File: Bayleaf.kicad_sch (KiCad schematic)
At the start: 68 parts, among them SW1 SW_SPDT, U1 Nice_Nano_V2

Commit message: v1 power management
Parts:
- added J1: Conn_01x02_Socket, Connector_PinHeader_2.54mm:PinHeader_1x02_P2.54mm_Vertical, symbol Connector:Conn_01x02_Socket
- added J2: Conn_01x02_Socket, Connector_JST:JST_SH_SM02B-SRSS-TB_1x02-1MP_P1.00mm_Horizontal, symbol Connector:Conn_01x02_Socket
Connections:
- net GND: now reaches U1.23 (GND)
- net GND: now also U1.3 (GND), U1.4 (GND), J1.1 (Pin_1), J2.2 (Pin_2)
- net +BATT: now reaches U1.24 (B+)
- net +BATT: now also SW1.2 (B)
- net at SW1.3 (C): now also J1.2 (Pin_2), J2.1 (Pin_1)
- no-connect marks 0 -> 1
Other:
- moved on the sheet: H1, H2, H3, H4, H5, H6

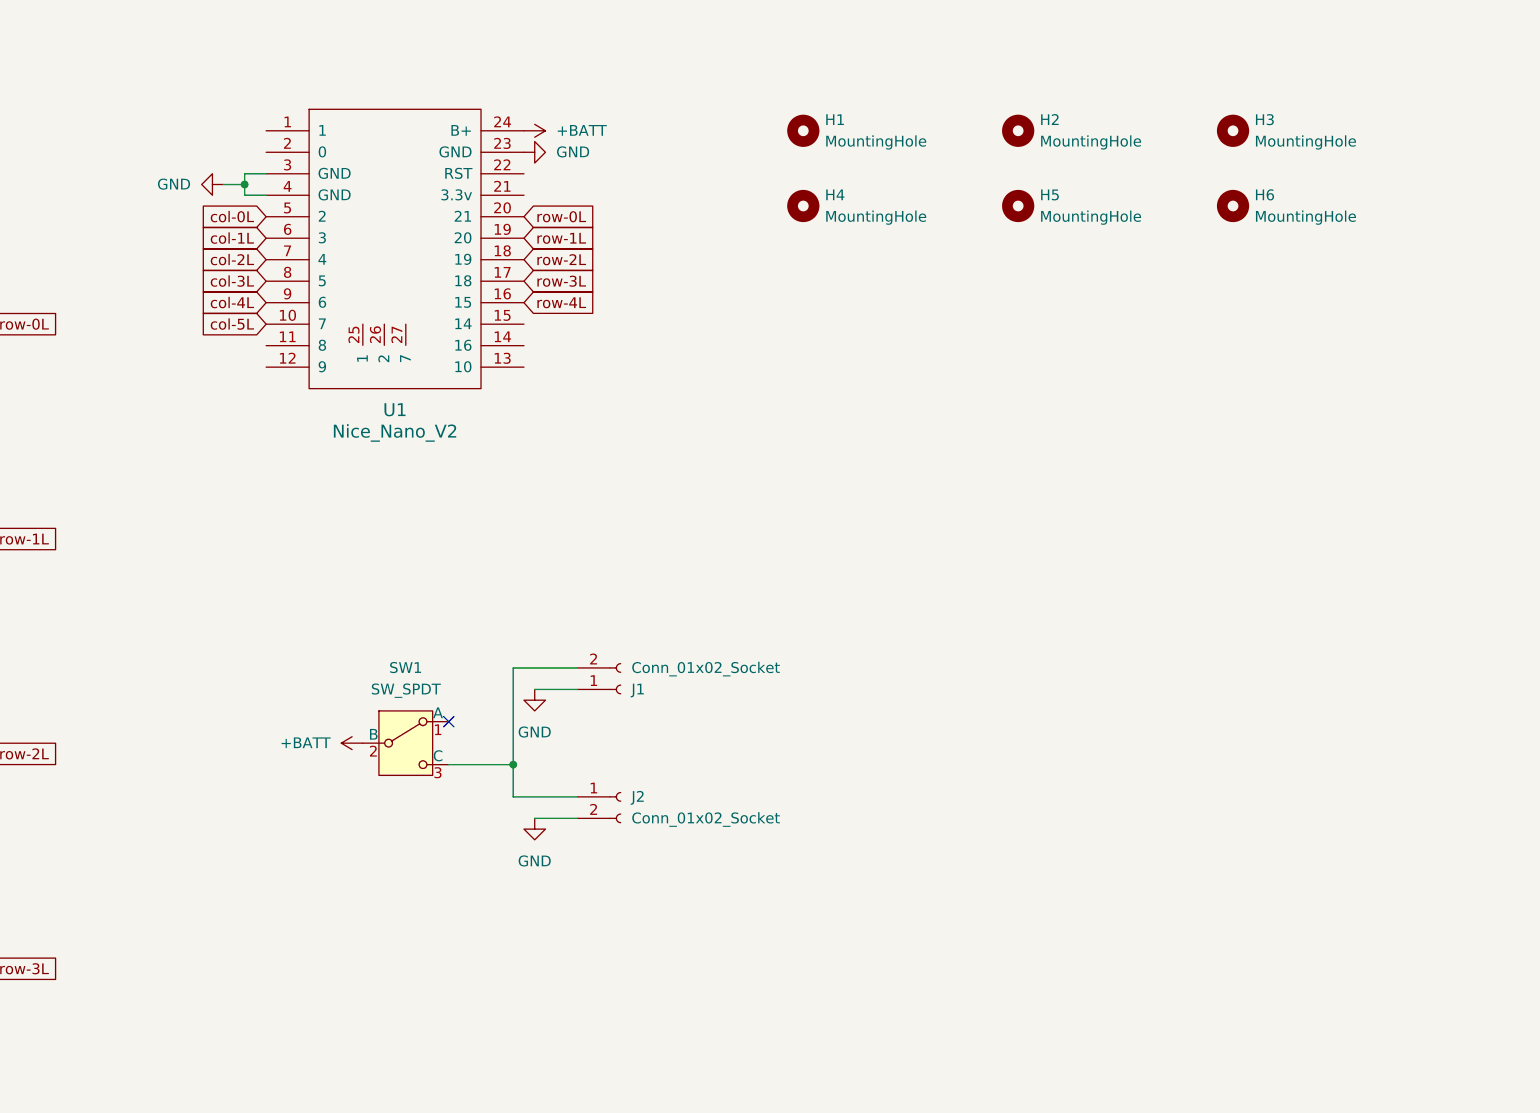
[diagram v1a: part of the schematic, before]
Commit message: Add rst, flags, logo, mounting hole
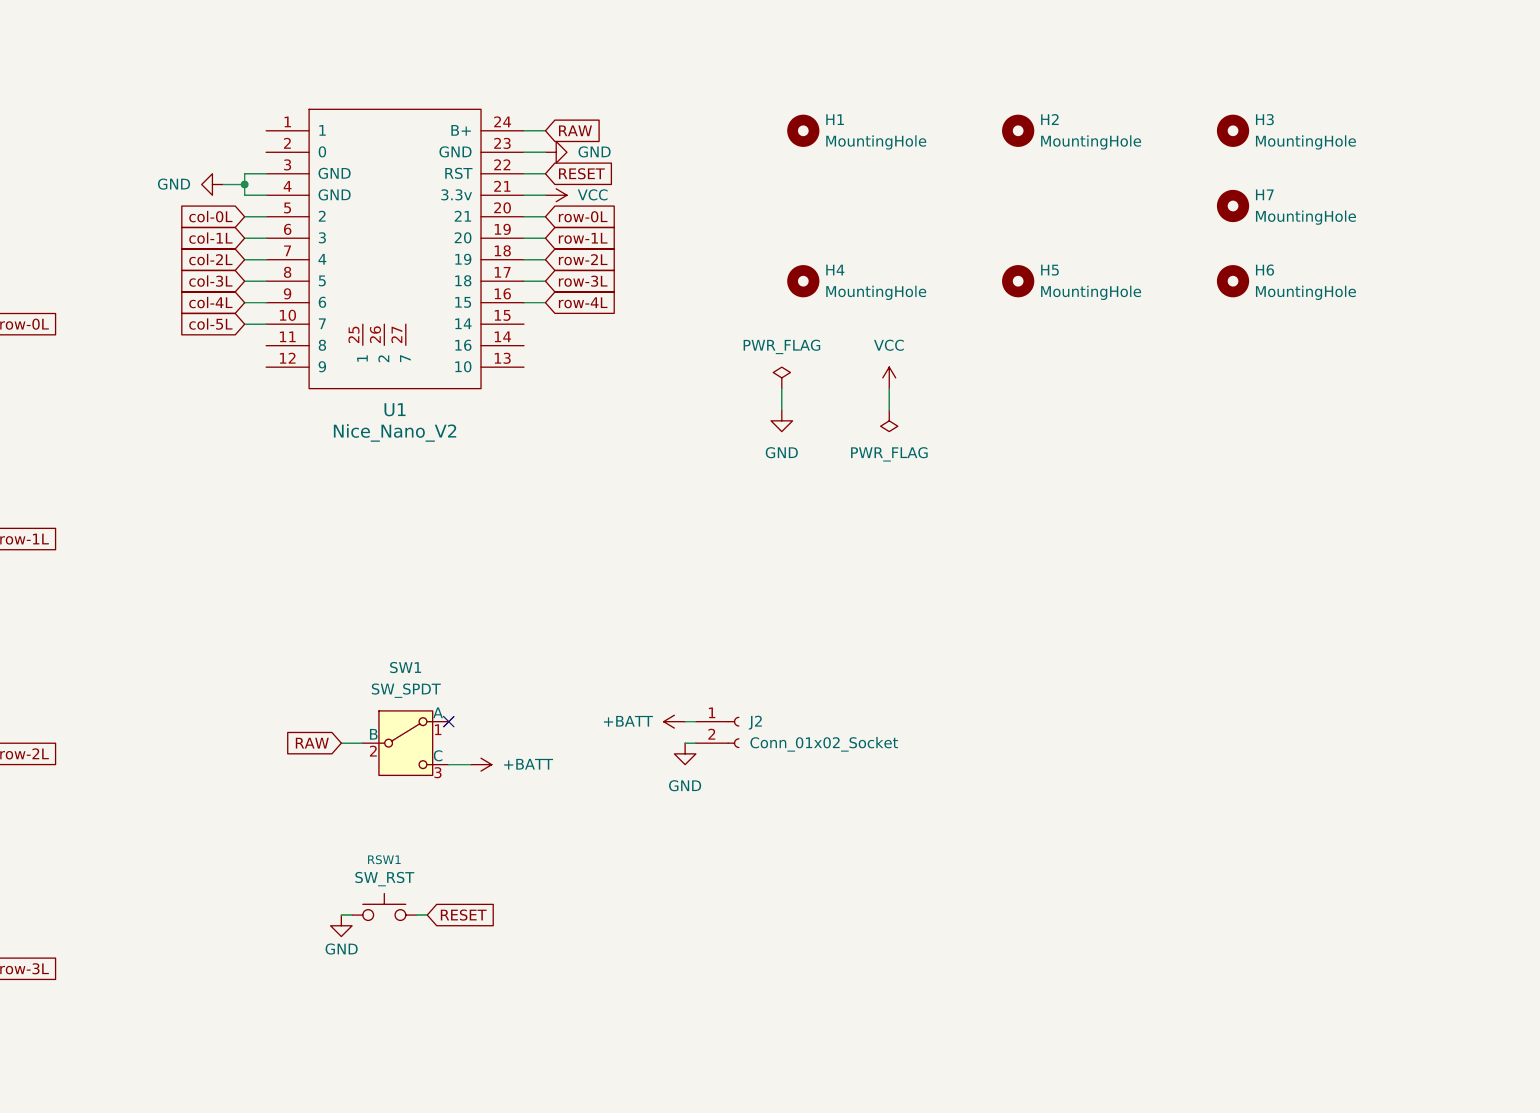
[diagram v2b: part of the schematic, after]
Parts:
- removed J1: Conn_01x02_Socket, Connector_PinHeader_2.54mm:PinHeader_1x02_P2.54mm_Vertical, symbol Connector:Conn_01x02_Socket
- added H7: MountingHole, MountingHole:MountingHole_2.2mm_M2, symbol Mechanical:MountingHole
- added RSW1: SW_RST, Button_Switch_SMD:SW_Tactile_SPST_NO_Straight_CK_PTS636Sx25SMTRLFS, symbol Lily58_Pro-rescue:SW_RST-Lily58-cache
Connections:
- net +BATT: now also J2.1 (Pin_1), SW1.3 (C); no longer SW1.2 (B), U1.24 (B+)
- net GND: now also RSW1.1
- net VCC: now reaches U1.21 (3.3v)
- net RESET: now reaches U1.22 (RST)
- net RESET: now also RSW1.2
- new net RAW: SW1.2 (B), U1.24 (B+)
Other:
- moved on the sheet: H4, H5, H6, J2
